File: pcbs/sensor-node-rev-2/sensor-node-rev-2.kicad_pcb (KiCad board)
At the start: 2 copper layers, 88 x 65 mm, 80 parts, among them IC1 NPP-301A-700AT, J2 DEBUG_CONN, J3 SMA EDGE CONN, J4 UART_CONN, J5 USER_CAP, SW1 SW_Push, U1 STM32U031R8T6, U2 nRF24L01P, U3 INA333xxDGK In-Amp, U4 TLV9001IDCK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

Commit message: Use new microcontroller package and remove some jumpers
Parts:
- removed C11, C19, C20, C21: EEE-FP0J102AL, libtpms:EEETC1V470P
- removed JP1: BOOT0 SEL, Connector_PinHeader_2.54mm:PinHeader_1x03_P2.54mm_Vertical
- removed JP12: RESET_EN, Jumper:SolderJumper-2_P1.3mm_Open_RoundedPad1.0x1.5mm
- removed S2: AYZ0102AGRLC, libtpms:AYZ0102AGRLC
- removed SW1: SW_Push, Button_Switch_SMD:SW_SPST_Omron_B3FS-100xP
- removed U3: INA333xxDGK In-Amp, Package_SO:VSSOP-8_3.0x3.0mm_P0.65mm
- removed X1: 16MHz, libtpms:830064296
- added C22: 100n, Capacitor_SMD:C_0402_1005Metric, F.Cu at (79.8, 129.2)
- added IC2: AD8226ARMZ, libtpms:SOP65P490X110-8N, F.Cu at (83.6, 133.8)
- added JP2: BOOT_SEL, Jumper:SolderJumper-3_P1.3mm_Open_RoundedPad1.0x1.5mm, F.Cu at (85.3, 121.3)
- added S3: CAS-120A1, libtpms:CAS120A1, F.Cu at (103.7, 107.5)
- added S4: Pushbutton switch, libtpms:TS2134035BK160SMTTR, F.Cu at (77.8, 132.8)
- added S5: CAS-120A1, libtpms:CAS120A1, F.Cu at (97.2, 112.8)
- added Y1: Crystal_16MHz, libtpms:830064296, F.Cu at (89.5, 112.4)
- C1, C5, C6, C8: value 100n -> C_Polarized; footprint Capacitor_SMD:C_0603_1608Metric -> libtpms:CAPPM7362X375N
- C2, C23, C24, C3, C4, C7: footprint Capacitor_SMD:C_0603_1608Metric -> Capacitor_SMD:C_0402_1005Metric
- D1, D2: footprint LED_SMD:LED_0603_1608Metric -> LED_SMD:LED_0402_1005Metric
- R1, R10, R11, R13, R14, R2, R3, R4, R5, R6, R7: footprint Resistor_SMD:R_0603_1608Metric -> Resistor_SMD:R_0402_1005Metric
- S1: value 206-124 -> CAS-120A1; footprint libtpms:206124 -> libtpms:CAS120A1
- U1: value STM32U031R8T6 -> STM32U031K8U6; footprint libtpms:LQFP64_STM -> libtpms:QFN50P500X500X60-33N-D
- moved H1 132.1 mm to (-82.1, 122.7)
- moved TP13 123.3 mm to (-99.0, 134.3)
- moved S1 122.9 mm to (103.7, 115.1), turned to 90 degrees
- moved TP10 121.9 mm to (-103.1, 133.6)
- moved TP11 121.9 mm to (-99.0, 121.5)
- moved TP12 121.9 mm to (-99.0, 125.5)
- moved TP5 121.9 mm to (-103.1, 121.5)
- moved TP6 121.9 mm to (-103.1, 125.5)
- moved TP9 121.9 mm to (-103.1, 129.6)
- moved TP1 121.9 mm to (-107.1, 121.5)
- moved TP15 121.9 mm to (-95.0, 121.5)
- moved TP16 121.9 mm to (-95.0, 125.5)
- moved TP17 121.9 mm to (-95.0, 129.6)
- moved TP18 121.9 mm to (-95.0, 133.6)
- moved TP2 121.9 mm to (-107.1, 125.5)
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- renumbered L2 to L1, L1 to L2
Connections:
- net Net-(AE1-A) renamed /NRF_ANT
- C1 pad 1: VDD -> Net-(JP11-A)
- C5 pad 1: VDD -> Net-(JP11-A)
- C6 pad 1: VDD -> Net-(JP11-A)
- C8 pad 1: /NRST -> Net-(JP11-A)
- JP11 pad 1: Net-(C11-+) -> Net-(JP11-A)
- PS1 pad 7: Net-(JP12-B) -> P2110B_RESET
- S1 pad 2: unconnected-(S1-Pad2) -> POWER_LED_EN
- S1 pad 3: unconnected-(S1-Pad3) -> GND
- U1 pad 11: PSENSE_MINUS -> USART1_TX
- U1 pad 12: GND -> P2110B_DOUT
- U1 pad 13: VDD -> USART1_RX
- U1 pad 16: unconnected-(U1-PA2-Pad16) -> GND
- U1 pad 17: P2110B_DOUT -> VDD
- U1 pad 18: GND -> P2110B_RESET
- U1 pad 19: VDD -> P2110B_DSET
- U1 pad 20: NRF_IRQ -> P2110B_INT
- U1 pad 21: NRF_SCK -> unconnected-(U1A-PA11[PA9]-Pad21)
- U1 pad 22: NRF_MISO -> /USER_LED
- U1 pad 23: NRF_MOSI -> SWDIO
- U1 pad 24: unconnected-(U1-PC4-Pad24) -> SWCLK
- U1 pad 25: NRF_CSN -> NRF_IRQ
- U1 pad 26: NRF_CE -> NRF_SCK
- U1 pad 27: unconnected-(U1-PB1-Pad27) -> NRF_MISO
- U1 pad 28: unconnected-(U1-PB2-Pad28) -> NRF_MOSI
- U1 pad 29: unconnected-(U1-PB10-Pad29) -> NRF_CSN
- U1 pad 30: /USER_LED -> NRF_CE
- U1 pad 31: GND -> /BOOT0
- U1 pad 32: VDD -> GND
- U1 pad 33: unconnected-(U1-PB12-Pad33) -> GND
- U1 pad 4: unconnected-(U1-PC15-OSC32_OUT-Pad4) -> /NRST
- U1 pad 5: unconnected-(U1-PF0-OSC_IN-Pad5) -> VDD
- U1 pad 6: unconnected-(U1-PF1-OSC_OUT-Pad6) -> PSENSE_OUT
- U1 pad 7: /NRST -> PSENSE_VREF
- U1 pad 8: PSENSE_OUT -> unconnected-(U1A-PA2-Pad8)
- U1 pad 9: PSENSE_VREF -> PSENSE_MINUS
- U2 pad 21: (no net) -> GND
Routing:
- net GND: vias 16 -> 5
- added copper zone on F.Cu, net /NRF_ANT
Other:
- board size 88 x 65 mm -> 55 x 49 mm
- board text removed: "2V5"
- board text removed: "BOOT0"
- board text removed: "CAP_SEL"
- board text removed: "DOUT_EN"
- board text removed: "DSET_EN"
- board text removed: "INT_EN"
- board text removed: "P2110B_VOUT"
- board text removed: "PWR_LED_EN"
- board text removed: "RESET_EN"
- board text removed: "UART"
- board text removed: "USART_RX"
- board text removed: "USART_TX"

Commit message: Finish routing and layout for sensor node rev 2
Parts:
- removed H1: MountingHole, MountingHole:MountingHole_2.2mm_M2_Pad
- removed J5: USER_CAP, Connector_PinSocket_2.54mm:PinSocket_1x02_P2.54mm_Vertical
- removed JP11: CAP_SEL, Connector_PinHeader_2.54mm:PinHeader_1x03_P2.54mm_Vertical
- removed S3: CAS-120A1, libtpms:CAS120A1
- added AE2: PCB Antenna, libtpms:TI_2G4_Inv_F_Antenna_1, F.Cu at (80.8, 97.0)
- added JP1: USER_LED_EN, Jumper:SolderJumper-2_P1.3mm_Open_RoundedPad1.0x1.5mm, F.Cu at (78.1, 122.2)
- R11, R14: value 17k -> 22k
- R4, R5: value 220R -> 470R
- TP1, TP10, TP11, TP12, TP2, TP3, TP4, TP5, TP6, TP9: footprint TestPoint:TestPoint_Pad_2.0x2.0mm -> TestPoint:TestPoint_Pad_1.5x1.5mm
- moved TP18 216.0 mm to (120.7, 121.4)
- moved TP16 215.7 mm to (120.7, 129.5)
- moved TP4 203.1 mm to (94.8, 111.8)
- moved TP3 202.5 mm to (94.8, 114.5)
- moved TP2 197.9 mm to (90.7, 120.8)
- moved TP14 195.4 mm to (96.3, 134.8), turned to -90 degrees
- moved TP1 195.2 mm to (88.0, 120.0)
- moved TP15 194.3 mm to (98.9, 108.1)
- moved TP13 192.3 mm to (93.3, 134.8), turned to -90 degrees
- moved TP17 191.0 mm to (94.7, 107.1)
- moved TP6 184.5 mm to (81.3, 118.7)
- moved TP10 183.0 mm to (79.9, 136.4)
- moved TP5 180.7 mm to (77.5, 117.8)
- moved TP9 179.7 mm to (76.6, 132.5)
- moved TP12 179.1 mm to (80.0, 132.5)
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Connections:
- C1 pad 1: Net-(JP11-A) -> VCAP
- C5 pad 1: Net-(JP11-A) -> VCAP
- C6 pad 1: Net-(JP11-A) -> VCAP
- C8 pad 1: Net-(JP11-A) -> VCAP
- D2 pad 1: USER_LED_EN -> Net-(D2-K)
- TP16 pad 1: Net-(TP16-Pad1) -> /P2110B_VOUT
- U1 pad 18: P2110B_RESET -> unconnected-(U1A-PA8-Pad18)
- U1 pad 21: unconnected-(U1A-PA11[PA9]-Pad21) -> P2110B_RESET
- U1 pad 22: /USER_LED -> unconnected-(U1A-PA12[PA10]-Pad22)
- U1 pad 3: unconnected-(U1A-PC15-OSC32_OUT-Pad3) -> /USER_LED
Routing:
- net VDD: track 0.00 -> 136.9 mm, vias 0 -> 7
- net SWDIO: track 0.00 -> 36.3 mm
- net SWCLK: track 0.00 -> 33.9 mm
- net PSENSE_PLUS: track 0.00 -> 33.5 mm
- net PSENSE_MINUS: track 0.00 -> 33.1 mm
- net /P2110B_VOUT: track 0.00 -> 30.9 mm
- net P2110B_RESET: track 0.00 -> 30.3 mm
- net NRF_MOSI: track 0.00 -> 28.6 mm, vias 0 -> 2
- net VCAP: track 0.00 -> 26.1 mm
- net NRF_MISO: track 0.00 -> 25.5 mm, vias 0 -> 2
- net NRF_CE: track 0.00 -> 23.6 mm
- net GND: track 0.00 -> 23.2 mm, vias 5 -> 79
- net +3.3V: track 0.00 -> 22.4 mm
- net PSENSE_OUT: track 0.00 -> 21.7 mm
- net PSENSE_VREF: track 0.00 -> 20.0 mm
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- removed copper zone on F.Cu, net /NRF_ANT
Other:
- board size 55 x 49 mm -> 49 x 49 mm
- board text added: "ANT"
- board text added: "BOOT0"
- board text added: "CE"
- board text added: "CLK"
- board text added: "CSN"
- board text added: "DIO"
- board text added: "EXT"
- board text added: "HARV"
- board text added: "IRQ"
- board text added: "ON"
- board text added: "OUT"
- board text added: "SB1"
- board text added: "SCK"
- board text added: "TL-81 Sensor Node (rev 2)"
- board text added: "ULED"
- board text added: "V+"
- board text added: "V-"
- board text added: "VCAP"
- board text added: "VOUT"
- board text added: "VREF"
- board text removed: "+"
- board text removed: "1"
- board text removed: "2V0"
- board text removed: "ADC_CH1"
- board text removed: "ADC_CH2"
- board text removed: "DEFAULT"
- board text removed: "LO"
- board text removed: "NRF_CE"
- board text removed: "NRF_CSN"
- board text removed: "NRF_IRQ"
- board text removed: "NRF_SCK"
- board text removed: "NRST"
- board text removed: "NRST_SW"
- board text removed: "PSENSE+"
- board text removed: "PSENSE-"
- board text removed: "SENSOR"
- board text removed: "SWDCLK"
- board text removed: "SWDIO"
- board text removed: "TL-81 Sensor Node (rev 1)"
- board text removed: "USER"
- board text removed: "USER_CAP"
- board text removed: "USER_LED_EN"
- board text removed: "[HI]"
- board text removed: "nRF24L01"

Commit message: Finalize rev 2 for manufacturing
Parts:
- moved C16 0.21 mm to (82.8, 103.2)
- moved C15 0.12 mm to (83.3, 104.7)
- moved L1 0.05 mm to (83.8, 108.2)
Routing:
- net GND: track 23.2 -> 25.3 mm, vias 79 -> 86
- net /NRF_ANT: track 1.95 -> 2.48 mm

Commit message: Add footprint and back silkscreen
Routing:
- net VDD: track 136.9 -> 136.0 mm
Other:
- board text added: "2024-07"
- board text added: "Mihir Nimgade"

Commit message: Add BOM and initial manufacturing files
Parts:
- R13: value 100k -> 49.9k
- R3: value ? -> 4.3M
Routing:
- net PSENSE_MINUS: track 33.1 -> 33.6 mm
- net GND: vias 86 -> 82

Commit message: Add little guy on back silkscreen and update manufacturing files
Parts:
- added G***: LOGO, LOGO, B.Cu at (112.6, 109.8)

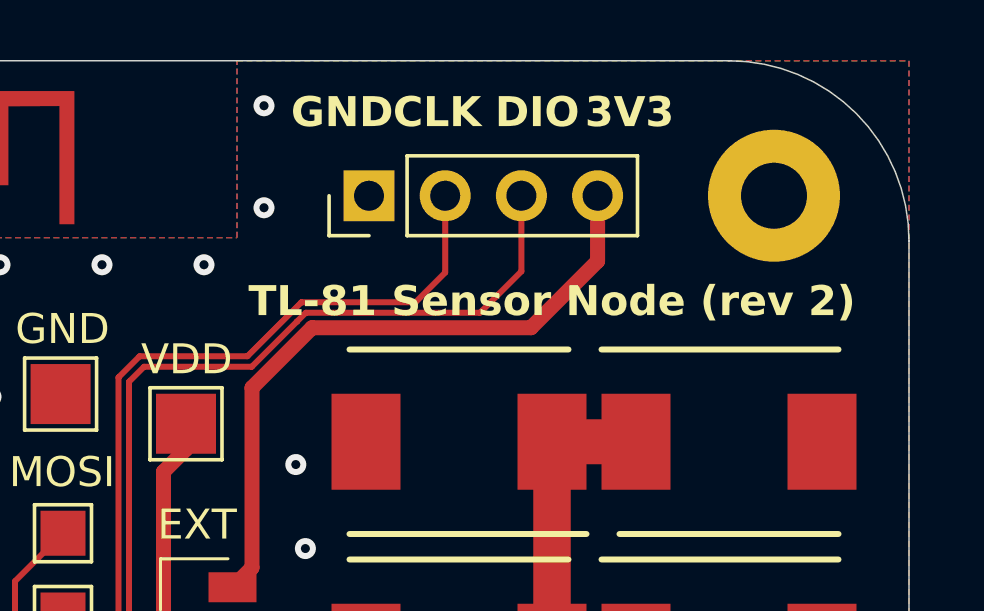
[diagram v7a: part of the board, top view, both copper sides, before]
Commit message: Update silkscreen and manu files for rev 2
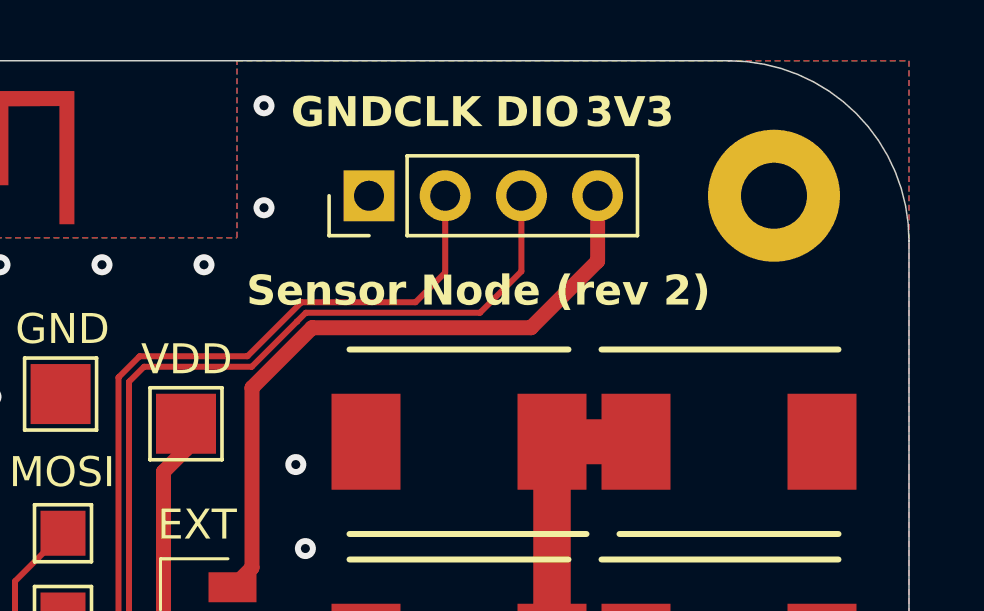
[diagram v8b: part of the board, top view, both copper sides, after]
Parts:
- moved G*** 5.92 mm to (116.2, 114.5)
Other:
- board text added: "Sensor Node (rev 2)"
- board text added: "Sensor Node Mihir Nimgade 2024-07"
- board text removed: "2024-07"
- board text removed: "Mihir Nimgade"
- board text removed: "TL-81 Sensor Node (rev 2)"
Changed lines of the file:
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@@
 	(footprint "LOGO"
 		(layer "B.Cu")
-		(at 112.6 109.85 180)
+		(at 116.2 114.55 180)
 		(property "Reference" "G***"
 			(at -4.4 2 180)
@@
 		(layer "Edge.Cuts")
 	)
-	(gr_text "2024-07"
-		(at 117.9365 115.269522 -90)
-		(layer "B.SilkS")
-		(effects
-			(font
-				(size 1 1)
-				(thickness 0.15)
-				(bold yes)
-			)
-			(justify left bottom mirror)
-		)
-	)
-	(gr_text "Mihir Nimgade"
-		(at 119.7765 115.269522 -90)
+	(gr_text "Sensor Node\nMihir Nimgade\n2024-07"
+		(at 120.65 108.7 0)
 		(layer "B.SilkS")
 		(effects
@@
 		)
 	)
-	(gr_text "TL-81 Sensor Node (rev 2)"
-		(at 111.1 104.6 0)
+	(gr_text "Sensor Node (rev 2)"
+		(at 108.65 104.25 0)
 		(layer "F.SilkS")
 		(effects
@@
 	)
 	(zone
-		(net 23)
-		(net_name "Net-(JP5-B)")
+		(net 26)
+		(net_name "Net-(JP9-B)")
 		(layer "F.Cu")
 		(name "$teardrop_padvia$")
 		(hatch full 0.1)
-		(priority 30010)
+		(priority 30008)
 		(attr
 			(teardrop
@@
 		(polygon
 			(pts
-				(xy 114.573907 133.731985) (xy 114.432485 133.873407) (xy 114.197 134.3015) (xy 114.832707 135.254707)
-				(xy 115.267538 134.3015)
+				(xy 108.098 122.8715) (xy 108.298 122.8715) (xy 108.845106 122.2365) (xy 108.228 121.283) (xy 107.593 122.2365)
 			)
 		)
 	)
 	(zone
-		(net 29)
-		(net_name "SWDIO")
+		(net 2)
+		(net_name "+3.3V")
 		(layer "F.Cu")
 		(name "$teardrop_padvia$")
 		(hatch full 0.1)
-		(priority 30003)
+		(priority 30001)
 		(attr
 			(teardrop
@@
 		(polygon
 			(pts
-				(xy 109.98 102.2) (xy 110.18 102.2) (xy 110.865298 100.825281) (xy 110.08 100.499) (xy 109.294702 100.825281)
+				(xy 112.37 102.2) (xy 112.87 102.2) (xy 113.405298 100.825281) (xy 112.62 100.499) (xy 111.834702 100.825281)
 			)
 		)
@@
 	)
 	(zone
-		(net 2)
-		(net_name "+3.3V")
-		(layer "F.Cu")
-		(name "$teardrop_padvia$")
-		(hatch full 0.1)
-		(priority 30001)
-		(attr
-			(teardrop
-				(type padvia)
-			)
-		)
-		(connect_pads yes
-			(clearance 0)
-		)
-		(min_thickness 0.0254)
-		(filled_areas_thickness no)
-		(fill yes
-			(thermal_gap 0.5)
-			(thermal_bridge_width 0.5)
-			(island_removal_mode 1)
-			(island_area_min 10)
-		)
-		(polygon
-			(pts
-				(xy 112.37 102.2) (xy 112.87 102.2) (xy 113.405298 100.825281) (xy 112.62 100.499) (xy 111.834702 100.825281)
-			)
-		)
-	)
-	(zone
 		(net 0)
 		(net_name "")
@@
 		(net_name "GND")
 		(layer "F.Cu")
+		(name "$teardrop_padvia$")
+		(hatch full 0.1)
+		(priority 30012)
+		(attr
+			(teardrop
+				(type padvia)
+			)
+		)
+		(connect_pads yes
+			(clearance 0)
+		)
+		(min_thickness 0.0254)
+		(filled_areas_thickness no)
+		(fill yes
+			(thermal_gap 0.5)
+			(thermal_bridge_width 0.5)
+			(island_removal_mode 1)
+			(island_area_min 10)
+		)
+		(polygon
+			(pts
+				(xy 111.75 122.1) (xy 111.25 122.1) (xy 111.084254 122.827792) (xy 111.5 123.001) (xy 111.915746 122.827792)
+			)
+		)
+	)
+	(zone
+		(net 1)
+		(net_name "GND")
+		(layer "F.Cu")
 		(hatch edge 0.5)
 		(priority 2)
@@
 	)
 	(zone
-		(net 53)
-		(net_name "/P2110B_VOUT")
+		(net 50)
+		(net_name "/VSET")
 		(layer "F.Cu")
 		(name "$teardrop_padvia$")
 		(hatch full 0.1)
-		(priority 30005)
+		(priority 30011)
 		(attr
 			(teardrop
@@
 		(polygon
 			(pts
-				(xy 109.460764 119.705711) (xy 109.107211 120.059264) (xy 109.244 121.412337) (xy 109.879707 121.284707)
-				(xy 110.164676 120.3315)
+				(xy 112.880834 119.779412) (xy 112.739412 119.920834) (xy 112.546 120.3315) (xy 113.181707 121.284707)
+				(xy 113.590764 120.3315)
 			)
 		)
@@
 	)
 	(zone
-		(net 1)
-		(net_name "GND")
+		(net 29)
+		(net_name "SWDIO")
 		(layer "F.Cu")
 		(name "$teardrop_padvia$")
 		(hatch full 0.1)
-		(priority 30012)
+		(priority 30003)
 		(attr
 			(teardrop
@@
 		(polygon
 			(pts
-				(xy 111.75 122.1) (xy 111.25 122.1) (xy 111.084254 122.827792) (xy 111.5 123.001) (xy 111.915746 122.827792)
+				(xy 109.98 102.2) (xy 110.18 102.2) (xy 110.865298 100.825281) (xy 110.08 100.499) (xy 109.294702 100.825281)
 			)
 		)
 	)
 	(zone
-		(net 48)
-		(net_name "Net-(J4-Pin_1)")
+		(net 24)
+		(net_name "Net-(JP6-B)")
 		(layer "F.Cu")
 		(name "$teardrop_padvia$")
 		(hatch full 0.1)
-		(priority 30000)
+		(priority 30006)
 		(attr
 			(teardrop
@@
 		(polygon
 			(pts
-				(xy 93.91 140.407695) (xy 93.71 140.407695) (xy 94.07 142.267891) (xy 94.92 142.001) (xy 95.363072 141.15)
+				(xy 113.281 133.6665) (xy 113.081 133.6665) (xy 112.546 134.3015) (xy 113.181 135.255) (xy 113.816 134.3015)
 			)
 		)
 	)
 	(zone
-		(net 49)
-		(net_name "Net-(J4-Pin_2)")
+		(net 25)
+		(net_name "SWCLK")
 		(layer "F.Cu")
 		(name "$teardrop_padvia$")
 		(hatch full 0.1)
-		(priority 30004)
+		(priority 30002)
 		(attr
 			(teardrop
@@
 		(polygon
 			(pts
-				(xy 96.328629 140.727208) (xy 96.187208 140.868629) (xy 96.674702 142.325281) (xy 97.460707 142.000707)
-				(xy 97.785281 141.214702)
+				(xy 107.44 102.2) (xy 107.64 102.2) (xy 108.325298 100.825281) (xy 107.54 100.499) (xy 106.754702 100.825281)
 			)
 		)
 	)
 	(zone
-		(net 50)
-		(net_name "/VSET")
+		(net 53)
+		(net_name "/P2110B_VOUT")
 		(layer "F.Cu")
 		(name "$teardrop_padvia$")
 		(hatch full 0.1)
-		(priority 30011)
+		(priority 30005)
 		(attr
 			(teardrop
@@
 		(polygon
 			(pts
-				(xy 112.880834 119.779412) (xy 112.739412 119.920834) (xy 112.546 120.3315) (xy 113.181707 121.284707)
-				(xy 113.590764 120.3315)
+				(xy 109.460764 119.705711) (xy 109.107211 120.059264) (xy 109.244 121.412337) (xy 109.879707 121.284707)
+				(xy 110.164676 120.3315)
 			)
 		)
 	)
 	(zone
-		(net 53)
-		(net_name "/P2110B_VOUT")
+		(net 48)
+		(net_name "Net-(J4-Pin_1)")
 		(layer "F.Cu")
 		(name "$teardrop_padvia$")
 		(hatch full 0.1)
-		(priority 30007)
+		(priority 30000)
 		(attr
 			(teardrop
@@
 		(polygon
 			(pts
-				(xy 109.77647 123.017522) (xy 110.130022 122.66397) (xy 110.514 122.2365) (xy 109.878293 121.283293)
-				(xy 109.288431 122.2365)
+				(xy 93.91 140.407695) (xy 93.71 140.407695) (xy 94.07 142.267891) (xy 94.92 142.001) (xy 95.363072 141.15)
 			)
 		)
 	)
 	(zone
-		(net 25)
-		(net_name "SWCLK")
+		(net 53)
+		(net_name "/P2110B_VOUT")
 		(layer "F.Cu")
 		(name "$teardrop_padvia$")
 		(hatch full 0.1)
-		(priority 30002)
+		(priority 30007)
 		(attr
 			(teardrop
@@
 		(polygon
 			(pts
-				(xy 107.44 102.2) (xy 107.64 102.2) (xy 108.325298 100.825281) (xy 107.54 100.499) (xy 106.754702 100.825281)
+				(xy 109.77647 123.017522) (xy 110.130022 122.66397) (xy 110.514 122.2365) (xy 109.878293 121.283293)
+				(xy 109.288431 122.2365)
 			)
 		)
@@
 	)
 	(zone
-		(net 26)
-		(net_name "Net-(JP9-B)")
+		(net 49)
+		(net_name "Net-(J4-Pin_2)")
 		(layer "F.Cu")
 		(name "$teardrop_padvia$")
 		(hatch full 0.1)
-		(priority 30008)
+		(priority 30004)
 		(attr
 			(teardrop
@@
 		(polygon
 			(pts
-				(xy 108.098 122.8715) (xy 108.298 122.8715) (xy 108.845106 122.2365) (xy 108.228 121.283) (xy 107.593 122.2365)
+				(xy 96.328629 140.727208) (xy 96.187208 140.868629) (xy 96.674702 142.325281) (xy 97.460707 142.000707)
+				(xy 97.785281 141.214702)
 			)
 		)
 	)
 	(zone
-		(net 24)
-		(net_name "Net-(JP6-B)")
+		(net 23)
+		(net_name "Net-(JP5-B)")
 		(layer "F.Cu")
 		(name "$teardrop_padvia$")
 		(hatch full 0.1)
-		(priority 30006)
+		(priority 30010)
 		(attr
 			(teardrop
@@
 		(polygon
 			(pts
-				(xy 113.281 133.6665) (xy 113.081 133.6665) (xy 112.546 134.3015) (xy 113.181 135.255) (xy 113.816 134.3015)
+				(xy 114.573907 133.731985) (xy 114.432485 133.873407) (xy 114.197 134.3015) (xy 114.832707 135.254707)
+				(xy 115.267538 134.3015)
 			)
 		)
@@
 	)
 	(group ""
-		(members "021875be-96e1-4bb9-9897-20d173c9e8c3" "dd223203-c01e-4c73-9256-f170c11f9872")
+		(members "dd223203-c01e-4c73-9256-f170c11f9872")
 	)
 )
